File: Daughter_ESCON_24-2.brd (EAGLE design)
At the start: 37.9 x 39.3 mm, 31 parts

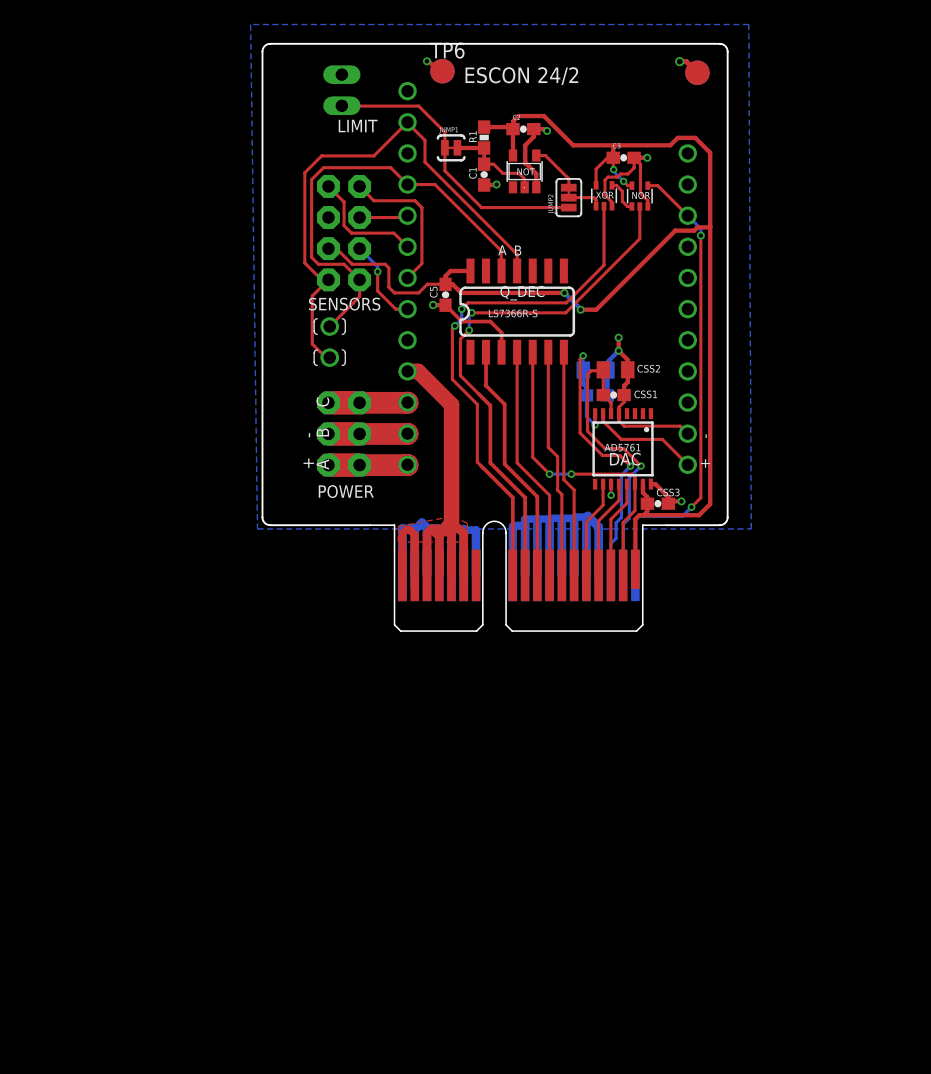
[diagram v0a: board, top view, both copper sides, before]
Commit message: Protection circuitry added but not routed
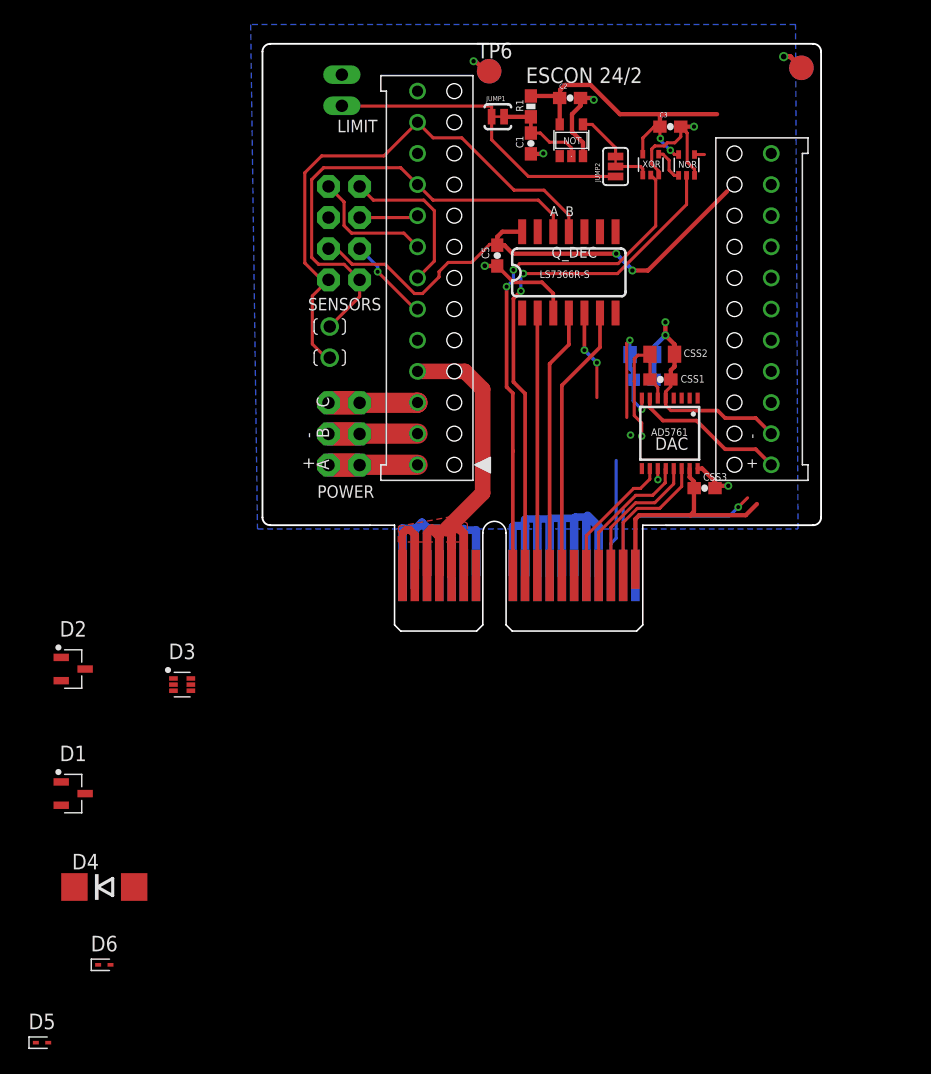
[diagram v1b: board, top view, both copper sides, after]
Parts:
- added D1, D2: 24V, Cannula_1_0:SOT95P230X110-3
- added D3: 14.2V, Cannula_1_0:SOTFL50P160X60-6
- added D4: 33V, Cannula_1_0:DO214AA
- added D5, D6: 3.3V, Cannula_1_0:SODFL1006X40
- ESCON_24-2: value ESCON_MODULE_24-2 -> ESCON_MODULE24-2_BOTTOM_ENTRY; device Cannula_1_0:ESCON_24-2 -> Cannula_1_0:ESCON_24-2_BOTTOM_ENTRY
- moved TP4 8.49 mm to (44.2, 46.5)
- moved TP5 8.49 mm to (44.2, 46.5)
- moved Q_DEC 5.29 mm to (25.8, 29.8)
- moved C5 5.29 mm to (19.4, 31.2)
- moved U$4 4.58 mm to (28.9, 44.8)
- moved C2 4.58 mm to (25.3, 44.0)
- moved C3 4.58 mm to (33.5, 41.7)
- moved NOR 4.58 mm to (34.8, 38.6)
- moved JUMP1 4.58 mm to (19.4, 42.5)
- moved C1 4.58 mm to (22.1, 40.3)
- moved JUMP2 4.58 mm to (29.0, 38.5)
- moved NOT 4.58 mm to (25.4, 40.6)
- moved R1 4.58 mm to (22.1, 43.4)
- moved XOR 4.58 mm to (31.9, 38.6)
- moved CSS1 4.02 mm to (32.7, 21.1)
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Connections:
- removed net CURR: ESCON_24-2.P$20
- removed net N$22: ESCON_24-2.P$11
- removed net N$24: ESCON_24-2.P$13
- removed net N$31: ESCON_24-2.P$22
- removed net N$32: ESCON_24-2.P$21
- removed net N$34: ESCON_24-2.P$19
- new net !AIN2: D1.2, ESCON_24-2.P$21
- new net !ENC_A: D3.3, ESCON_24-2.P$11
- new net !ENC_B: D3.6, ESCON_24-2.P$13
- new net AIN2: D1.1, ESCON_24-2.P$22
- new net AOUT1: D6.2, ESCON_24-2.P$20
- new net AOUT2: D5.2, ESCON_24-2.P$19
- net 24V: now also D4.C
- net AGND: now also D2.2
- net ENC_A: now also D3.1
- net ENC_B: now also D3.4
- net GND: now also D1.3, D2.3, D3.2, D3.5, D4.A, D5.1, D6.1
- net VOUT_DAC: now also D2.1
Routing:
- net 3.3V: track 113.1 -> 87.5 mm
- net ENABLE_M1: track 38.4 -> 15.3 mm, vias 2 -> 1
- net MOSI: track 18.6 -> 0.00 mm
- net -15V: track 25.0 -> 17.3 mm
- net SCLK: track 26.0 -> 19.1 mm
- net +15V: track 28.2 -> 22.9 mm
- net MISO: track 18.7 -> 22.7 mm
- net SYNC: track 7.99 -> 11.8 mm
- net SDI01: track 8.14 -> 11.8 mm
- net VOUT_DAC: track 9.00 -> 12.6 mm
- net 24V: track 41.2 -> 44.8 mm
- net AGND: track 16.4 -> 19.9 mm
- net SDI12: track 8.01 -> 11.2 mm
- net ENC_A: track 36.2 -> 38.9 mm
- net SS1: track 19.3 -> 22.1 mm
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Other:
- board size 37.9 x 39.3 mm -> 45.6 x 39.3 mm

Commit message: Finished and generated gerbers
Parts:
- D1: value 24V -> 33V; device Cannula_1_0:SOT95P230X110-3 -> Cannula_1_0:DO214AA
- D2: value 24V -> 14.2V; device Cannula_1_0:SOT95P230X110-3 -> Cannula_1_0:SOTFL50P160X60-6
- D3: value 14.2V -> 3.3V; device Cannula_1_0:SOTFL50P160X60-6 -> Cannula_1_0:SODFL1006X40
- D4: value 33V -> 3.3V; device Cannula_1_0:DO214AA -> Cannula_1_0:SODFL1006X40
- D5, D6: value 3.3V -> 24V; device Cannula_1_0:SODFL1006X40 -> Cannula_1_0:SOT95P230X110-3
- moved D5 84.9 mm to (47.0, 21.8)
- moved D4 74.7 mm to (45.8, 26.1), turned to 270 degrees
- moved D6 73.8 mm to (47.0, 16.7)
- moved D3 61.4 mm to (45.8, 28.6), turned to 270 degrees
- moved D2 52.4 mm to (19.2, 37.0), turned to 90 degrees
- moved D1 39.9 mm to (16.5, 11.4), turned to 180 degrees
- moved TP3 25.1 mm to (43.8, 46.5)
- moved TP6 25.1 mm to (43.8, 46.5)
- moved TP4 5.08 mm to (49.3, 46.5)
- moved TP5 5.08 mm to (49.3, 46.5)
- moved PCI_CARD 3.81 mm to (22.9, 9.19)
- moved U$3 1.69 mm to (26.6, 33.6)
- moved ESCON_24-2 1.27 mm to (27.3, 30.6)
- renumbered C5 to C4, JUMP1 to JP1, JUMP2 to JP2
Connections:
- net !AIN2: now also D5.1; no longer D1.2
- net !ENC_A: now also D2.3; no longer D3.3
- net !ENC_B: now also D2.4; no longer D3.6
- net 24V: now also D1.C; no longer D4.C
- net AGND: now also D6.1; no longer D2.2
- net AIN2: now also D5.2; no longer D1.1
- net AOUT1: now also D4.2; no longer D6.2
- net AOUT2: now also D3.2; no longer D5.2
- net ENC_A: now also D2.1; no longer D3.1
- net ENC_B: now also D2.6; no longer D3.4
- net GND: now also D1.A, D2.2, D2.5, D3.1, D4.1, D5.3, D6.3; no longer D1.3, D2.3, D3.2, D3.5, D4.A, D5.1, D6.1
- net VOUT_DAC: now also D6.2; no longer D2.1
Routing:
- net 3.3V: track 87.5 -> 142.9 mm
- net ENABLE_M1: track 15.3 -> 52.8 mm, vias 1 -> 2
- net MOSI: track 0.00 -> 22.1 mm
- net SCLK: track 19.1 -> 32.1 mm, vias 2 -> 0
- net !ENC_B: track 0.00 -> 12.4 mm
- net !ENC_A: track 0.00 -> 10.2 mm, vias 0 -> 2
- net -15V: track 17.3 -> 26.9 mm
- net MOTC: track 7.27 -> 15.6 mm
- net MOTA: track 7.27 -> 15.6 mm
- net MOTB: track 7.27 -> 15.1 mm
- net GND: track 112.1 -> 119.1 mm, vias 9 -> 16
- net +15V: track 22.9 -> 29.9 mm
- net AIN2: track 0.00 -> 4.48 mm
- net AGND: track 19.9 -> 24.3 mm
- net !AIN2: track 0.00 -> 4.40 mm
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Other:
- board size 45.6 x 39.3 mm -> 50.6 x 39.3 mm
- board text added: "3.3V"
- board text added: "5V"
- board text added: "ESCON Module 24/2"
- board text added: "GND"
- board text added: "H1"
- board text added: "H2"
- board text added: "November 2018"
- board text removed: "ESCON 24/2"

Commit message: Replaced 3.3V TVS with larger package
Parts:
- removed D3, D4: 3.3V, Cannula_1_0:SODFL1006X40
- added D7: 3.3V, Cannula_1_0:SOT95P230X110-3
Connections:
- net AOUT1: now also D7.2; no longer D4.2
- net AOUT2: now also D7.1; no longer D3.2
- net GND: now also D7.3; no longer D3.1, D4.1
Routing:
- net GND: track 119.1 -> 118.2 mm, vias 16 -> 15
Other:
- board text added: "August 2019"
- board text removed: "November 2018"
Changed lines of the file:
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@@
 <?xml version="1.0" encoding="utf-8"?>
 <!DOCTYPE eagle SYSTEM "eagle.dtd">
-<eagle version="9.2.2">
+<eagle version="9.3.1">
 <drawing>
 <settings>
@@
 <text x="2.7686" y="33.9598" size="0.6096" layer="21" font="vector" ratio="21">GND</text>
 <text x="19.6088" y="45.974" size="1.27" layer="21" ratio="13">ESCON Module 24/2</text>
-<text x="40.64" y="10.0076" size="0.8128" layer="21" ratio="19">November 2018</text>
+<text x="41.91" y="10.0076" size="0.8128" layer="21" ratio="19">August 2019</text>
 </plain>
 <attributes>
@@
 <attribute name="VALUE" x="17.7428" y="10.9744" size="0.4064" layer="27" ratio="10" rot="R90"/>
 </element>
-<element name="D4" library="Cannula_1_0" package="SODFL1006X40" package3d_urn="urn:adsk.eagle:package:6452786/1" value="3.3V" x="45.8216" y="26.0604" smashed="yes" rot="R270">
-<attribute name="NAME" x="46.99" y="26.1434" size="0.6096" layer="21" font="vector" ratio="21" align="bottom-center"/>
-<attribute name="VALUE" x="46.99" y="25.6354" size="0.3048" layer="27" rot="R180" align="top-center"/>
-</element>
-<element name="D3" library="Cannula_1_0" package="SODFL1006X40" package3d_urn="urn:adsk.eagle:package:6452786/1" value="3.3V" x="45.8216" y="28.6004" smashed="yes" rot="R270">
-<attribute name="NAME" x="46.99" y="28.6326" size="0.6096" layer="21" font="vector" ratio="21" align="bottom-center"/>
-<attribute name="VALUE" x="46.99" y="28.1754" size="0.3048" layer="27" rot="R180" align="top-center"/>
+<element name="D7" library="Cannula_1_0" package="SOT95P230X110-3" package3d_urn="urn:adsk.eagle:package:6452074/1" value="3.3V" x="46.99" y="26.8224" smashed="yes">
+<attribute name="NAME" x="46.99" y="28.6532" size="0.6096" layer="21" font="vector" ratio="21" align="bottom-center"/>
+<attribute name="VALUE" x="46.7168" y="26.8224" size="0.3048" layer="27" font="vector" rot="R270" align="top-center"/>
 </element>
 </elements>
@@
 <contactref element="D6" pad="3"/>
 <contactref element="D5" pad="3"/>
-<contactref element="D4" pad="1"/>
-<contactref element="D3" pad="1"/>
 <contactref element="D2" pad="2"/>
 <contactref element="D2" pad="5"/>
@@
 <wire x1="47.968" y1="22.644" x2="47.9552" y2="22.6568" width="0.3556" layer="1"/>
 <via x="47.9552" y="22.6568" extent="1-16" drill="0.381"/>
-<wire x1="45.8216" y1="26.5654" x2="44.961" y2="26.5654" width="0.3048" layer="1"/>
-<wire x1="44.961" y1="26.5654" x2="44.958" y2="26.5684" width="0.3048" layer="1"/>
-<via x="44.958" y="26.5684" extent="1-16" drill="0.3556"/>
-<wire x1="45.8216" y1="29.1054" x2="45.8186" y2="29.1084" width="0.3048" layer="1"/>
-<wire x1="45.8186" y1="29.1084" x2="44.958" y2="29.1084" width="0.3048" layer="1"/>
-<via x="44.958" y="29.1084" extent="1-16" drill="0.3556"/>
 <wire x1="19.2024" y1="37.7952" x2="19.2024" y2="38.7604" width="0.3048" layer="1"/>
+<contactref element="D7" pad="3"/>
+<wire x1="47.968" y1="26.8224" x2="47.968" y2="26.0732" width="0.3556" layer="1"/>
+<wire x1="47.968" y1="26.0732" x2="47.9552" y2="26.0604" width="0.3556" layer="1"/>
+<via x="47.9552" y="26.0604" extent="1-16" drill="0.381"/>
 </signal>
 <signal name="-15V">
@@
 <signal name="AOUT1">
 <contactref element="ESCON_24-2" pad="P$20"/>
-<contactref element="D4" pad="2"/>
-<wire x1="45.8186" y1="25.5524" x2="45.8216" y2="25.5554" width="0.3048" layer="1"/>
-<wire x1="41.7068" y1="25.5524" x2="45.8186" y2="25.5524" width="0.3048" layer="1"/>
+<contactref element="D7" pad="2"/>
+<wire x1="46.012" y1="25.8724" x2="42.0268" y2="25.8724" width="0.254" layer="1"/>
+<wire x1="42.0268" y1="25.8724" x2="41.7068" y2="25.5524" width="0.254" layer="1"/>
 </signal>
 <signal name="MOTA">
@@
 <signal name="AOUT2">
 <contactref element="ESCON_24-2" pad="P$19"/>
-<contactref element="D3" pad="2"/>
-<wire x1="45.8186" y1="28.0924" x2="45.8216" y2="28.0954" width="0.3048" layer="1"/>
-<wire x1="41.7068" y1="28.0924" x2="45.8186" y2="28.0924" width="0.3048" layer="1"/>
+<contactref element="D7" pad="1"/>
+<wire x1="46.012" y1="27.7724" x2="42.0268" y2="27.7724" width="0.254" layer="1"/>
+<wire x1="42.0268" y1="27.7724" x2="41.7068" y2="28.0924" width="0.254" layer="1"/>
 </signal>
 <signal name="AGND">
